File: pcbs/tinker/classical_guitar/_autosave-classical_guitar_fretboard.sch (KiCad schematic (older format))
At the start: 172 parts, among them U1 AT42QT1110-A, U2 AT42QT1110-A, U3 AT42QT1110-A

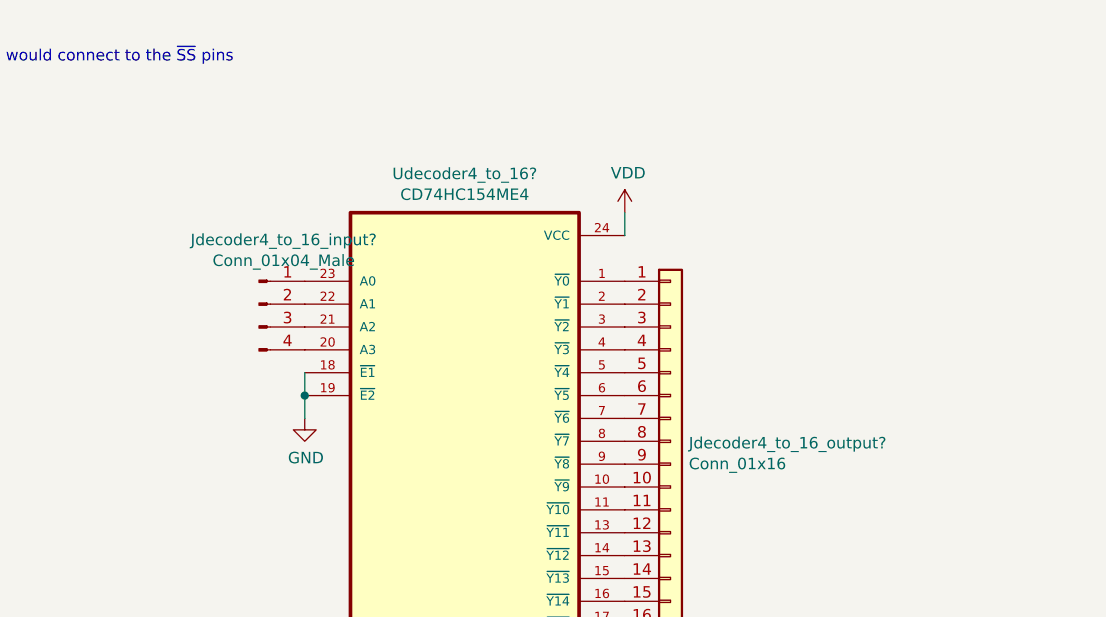
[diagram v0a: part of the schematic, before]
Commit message: Replaced 5-to-32 decoder with 4-to-16 decoder
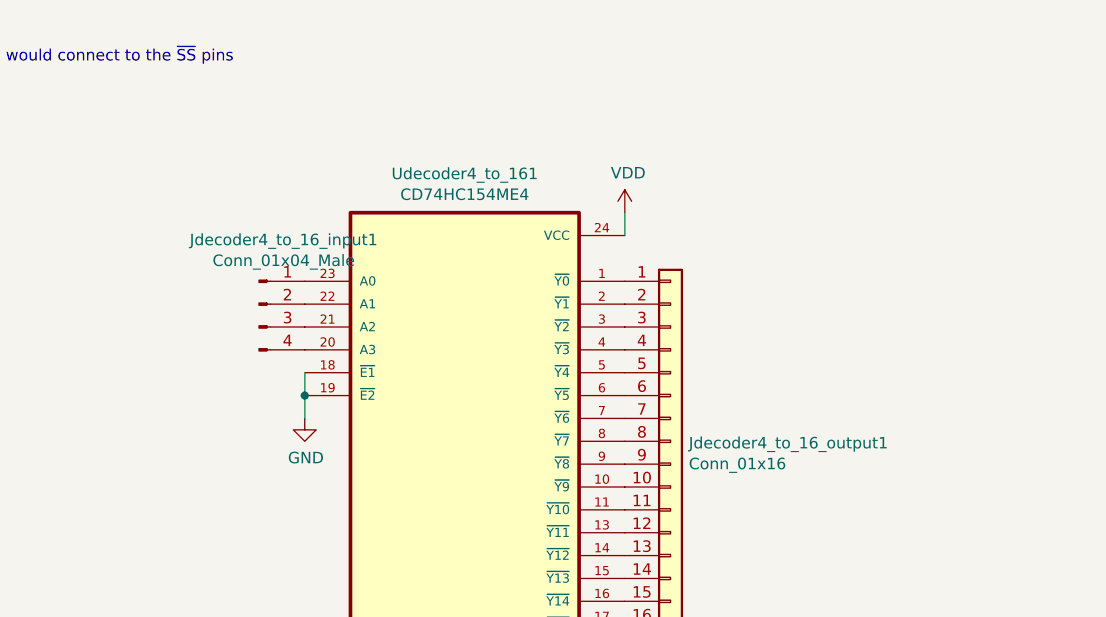
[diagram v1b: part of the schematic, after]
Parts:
- Jdecoder4_to_16_input1: renamed from Jdecoder4_to_16_input?; footprint (none) -> Connector_PinSocket_2.54mm:PinSocket_1x04_P2.54mm_Vertical
- Jdecoder4_to_16_output1: renamed from Jdecoder4_to_16_output?; footprint (none) -> Connector_PinSocket_2.54mm:PinSocket_1x16_P2.54mm_Vertical
- Udecoder4_to_161: renamed from Udecoder4_to_16?; footprint SOIC127P1030X265-24N -> Package_SO:SOIC-24W_7.5x15.4mm_P1.27mm
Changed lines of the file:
@@
 $EndComp
 $Comp
-L Custom_74xx:CD74HC154ME4 Udecoder4_to_16?
+L Custom_74xx:CD74HC154ME4 Udecoder4_to_161
 U 1 1 6445F660
 P 3950 6200
-F 0 "Udecoder4_to_16?" H 3950 7470 50  0000 C CNN
+F 0 "Udecoder4_to_161" H 3950 7470 50  0000 C CNN
 F 1 "CD74HC154ME4" H 3950 7379 50  0000 C CNN
-F 2 "SOIC127P1030X265-24N" H 3550 7350 50  0001 L BNN
+F 2 "Package_SO:SOIC-24W_7.5x15.4mm_P1.27mm" H 3550 7350 50  0001 L BNN
 F 3 "" H 3950 6200 50  0001 L BNN
 	1    3950 6200
@@
 $EndComp
 $Comp
-L power:GND #PWR?
+L power:GND #PWR021
 U 1 1 644A4F53
 P 3250 6000
-F 0 "#PWR?" H 3250 5750 50  0001 C CNN
+F 0 "#PWR021" H 3250 5750 50  0001 C CNN
 F 1 "GND" H 3255 5827 50  0000 C CNN
 F 2 "" H 3250 6000 50  0001 C CNN
@@
 	3250 5900 3250 6000
 $Comp
-L power:GND #PWR?
+L power:GND #PWR023
 U 1 1 644EA8EE
 P 4650 7300
-F 0 "#PWR?" H 4650 7050 50  0001 C CNN
+F 0 "#PWR023" H 4650 7050 50  0001 C CNN
 F 1 "GND" H 4655 7127 50  0000 C CNN
 F 2 "" H 4650 7300 50  0001 C CNN
@@
 	4650 7200 4650 7300
 $Comp
-L power:VDD #PWR?
+L power:VDD #PWR022
 U 1 1 6450E3BE
 P 4650 5100
-F 0 "#PWR?" H 4650 4950 50  0001 C CNN
+F 0 "#PWR022" H 4650 4950 50  0001 C CNN
 F 1 "VDD" H 4665 5273 50  0000 C CNN
 F 2 "" H 4650 5100 50  0001 C CNN
@@
 	4650 5100 4650 5200
 $Comp
-L Connector_Generic:Conn_01x16 Jdecoder4_to_16_output?
+L Connector_Generic:Conn_01x16 Jdecoder4_to_16_output1
 U 1 1 6453313E
 P 4850 6100
-F 0 "Jdecoder4_to_16_output?" H 4930 6092 50  0000 L CNN
+F 0 "Jdecoder4_to_16_output1" H 4930 6092 50  0000 L CNN
 F 1 "Conn_01x16" H 4930 6001 50  0000 L CNN
-F 2 "" H 4850 6100 50  0001 C CNN
+F 2 "Connector_PinSocket_2.54mm:PinSocket_1x16_P2.54mm_Vertical" H 4850 6100 50  0001 C CNN
 F 3 "~" H 4850 6100 50  0001 C CNN
 	1    4850 6100
@@
 $EndComp
 $Comp
-L Connector:Conn_01x04_Male Jdecoder4_to_16_input?
+L Connector:Conn_01x04_Male Jdecoder4_to_16_input1
 U 1 1 6455E6EE
 P 3050 5500
-F 0 "Jdecoder4_to_16_input?" H 3158 5781 50  0000 C CNN
+F 0 "Jdecoder4_to_16_input1" H 3158 5781 50  0000 C CNN
 F 1 "Conn_01x04_Male" H 3158 5690 50  0000 C CNN
-F 2 "" H 3050 5500 50  0001 C CNN
+F 2 "Connector_PinSocket_2.54mm:PinSocket_1x04_P2.54mm_Vertical" H 3050 5500 50  0001 C CNN
 F 3 "~" H 3050 5500 50  0001 C CNN
 	1    3050 5500
